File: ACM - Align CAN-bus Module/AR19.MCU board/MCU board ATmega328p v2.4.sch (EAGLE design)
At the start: 37 parts, among them IC1 ATMEGA328P-MMH, IC2 MIC5239-5.0YS_TR, IC3 MCP25625-E_ML, J1 AVR_SPI_PROG_3X2NS

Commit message: + SPI Priority | / 10K and 500Ohm to larger package | Smallest part 1206
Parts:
- removed C12, C13, C5, C6, C7, C8: 0.1uF, eagle-ltspice:CC0603
- removed R2: 10KΩ, CPF0201D10KC1:CPF0201D10KC1
- added C14, C15, C16, C17, C18, C19: 0.1uF_12, 12066D106KAT2A:12066D106KAT2A
- added R3, R4, R5: 500Ohm, CRCW1206499RFKEAHP(499ohm resistor):CRCW1206499RFKEAHP
- added R6: 10K Ohm, CRCW120610K0FKEAHP(10K Ohm):CRCW120610K0FKEAHP
- C11: value 0.1uF -> 0.1uF_12; device eagle-ltspice:CC0603 -> 12066D106KAT2A:12066D106KAT2A
- I/O_D2_INT: device wirepad:2,15/1,0 -> wirepad_edit:2,15/1,0(HALFHOLE)H+V
- R1: value 10KΩ -> 10K Ohm; device CPF0201D10KC1:CPF0201D10KC1 -> CRCW120610K0FKEAHP(10K Ohm):CRCW120610K0FKEAHP
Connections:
- removed net MISO: J1.1
- removed net MOSI: J1.4
- new net PROG_MISO: J1.1, R4.1
- new net PROG_MOSI: J1.4, R5.1
- new net PROG_SCK: J1.3, R3.1
- net 5V: now also C11.2, C14.2, C15.2, C17.2, C18.2, C19.2, R6.2; no longer C11.1, C12.1, C13.1, C6.1, C7.1, C8.1, R2.2
- net CAN_MISO: now also R4.2
- net CAN_MOSI: now also R5.2
- net GND: now also C11.1, C14.1, C15.1, C16.1, C17.1, C18.1, C19.1; no longer C11.2, C12.2, C13.2, C5.2, C6.2, C7.2, C8.2
- net MCP_RESET: now also C16.2, R1.1; no longer C5.1, R2.1
- net RESET_MCU: now also R6.1; no longer R1.1
- net SCK: now also R3.2; no longer J1.3
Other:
- note added: "SPI Priority"
- moved on the sheet: R1

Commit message: Updated BOM and SPI Priority
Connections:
- net CAN_MISO: now also R4.1; no longer IC1.(PCINT4/MISO)_PB4, R4.2
- net CAN_MOSI: now also R5.1; no longer IC1.(PCINT3/OC2A/MOSI)_PB3, R5.2
- net PROG_MISO: now also IC1.(PCINT4/MISO)_PB4, R4.2; no longer R4.1
- net PROG_MOSI: now also IC1.(PCINT3/OC2A/MOSI)_PB3, R5.2; no longer R5.1
- net PROG_SCK: now also IC1.PB5_(SCK/PCINT5), R3.2; no longer R3.1
- net SCK: now also R3.1; no longer IC1.PB5_(SCK/PCINT5), R3.2

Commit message: Byttet I/O pins, 0603 imp smd størrelse. Mangler dotstar support
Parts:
- removed C1, C4: 10uF, T491A106K016AT:T491A106K016AT
- removed C14, C15, C18, C19: 0.1uF_12, 12066D106KAT2A:12066D106KAT2A
- removed I/O_AD1, I/O_AD2, I/O_AD3, I/O_D0_RX, I/O_D1_TX, I/O_D2_INT: (no value), wirepad_edit:2,15/1,0(HALFHOLE)H+V
- removed R4, R5: 500Ohm, CRCW1206499RFKEAHP(499ohm resistor):CRCW1206499RFKEAHP
- removed R6: 10K Ohm, CRCW120610K0FKEAHP(10K Ohm):CRCW120610K0FKEAHP
- added C12, C13, C6, C7, C8: 0.1uF, eagle-ltspice:CC0603
- added C5: 22pF, eagle-ltspice:CC0603
- added D1: (no value), eagle-ltspice:DIODE_E-
- added I/O_PWM0_INT: I/O_PWM0_INT, wirepad_edit:2,15/1,0(HALFHOLE)H+V
- added I/O_PWM1: I/O_PWM1, wirepad_edit:2,15/1,0(HALFHOLE)H+V
- added I/O_PWM2: I/O_PWM2, wirepad_edit:2,15/1,0(HALFHOLE)H+V
- added MISO: MISO, wirepad_edit:2,15/1,0(HALFHOLE)H+V
- added MOSI: MOSI, wirepad_edit:2,15/1,0(HALFHOLE)H+V
- added SCK: SCK, wirepad_edit:2,15/1,0(HALFHOLE)H+V
- 12V: value (none) -> 12V
- C10: value 22pF -> 10uF; device 12066D106KAT2A:12066D106KAT2A -> eagle-ltspice:CC0603
- C11: value 0.1uF_12 -> 10uF; device 12066D106KAT2A:12066D106KAT2A -> eagle-ltspice:CC0603
- C16, C17: value 0.1uF_12 -> 0.1uF; device 12066D106KAT2A:12066D106KAT2A -> eagle-ltspice:CC0603
- C2, C3, C9: device 12066D106KAT2A:12066D106KAT2A -> eagle-ltspice:CC0603
- I/O_AD0: value (none) -> I/O_AD0
- I/O_CANH, I/O_CANL: value (none) -> I/O_CANH
- I/O_SCL_AD2: value (none) -> I/O_SCL_AD2
- I/O_SDA_AD1: value (none) -> I/O_SDA_AD1
- R1: value 10K Ohm -> 10kOhm; device CRCW120610K0FKEAHP(10K Ohm):CRCW120610K0FKEAHP -> eagle-ltspice:RR0603
- R3: value 500Ohm -> 10kOhm; device CRCW1206499RFKEAHP(499ohm resistor):CRCW1206499RFKEAHP -> eagle-ltspice:RR0603
- RES_PAD1: value (none) -> RES_PAD
- RES_PAD2: value (none) -> RES_PAD2
- renumbered I/O_AD4_SDA to I/O_SDA_AD1, I/O_AD5_SCL to I/O_SCL_AD2
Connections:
- net CAN_INIT renamed CAN_INT
- net I/O_AD4_SCL renamed N$6
- net I/O_AD5_SCL renamed N$7
- removed net CAN_MISO: IC3.SO, R4.1
- removed net CAN_MOSI: IC3.SI, R5.1
- removed net I/O_AD0: I/O_AD0.P, IC1.PC0_(ADC0/PCINT8)
- removed net I/O_AD1: I/O_AD1.P, IC1.PC1_(ADC1/PCINT9)
- removed net I/O_AD2: I/O_AD2.P, IC1.PC2_(ADC2/PCINT10)
- removed net I/O_AD3: I/O_AD3.P, IC1.PC3_(ADC3/PCINT11)
- removed net I/O_D0_RX: I/O_D0_RX.P, IC1.PD0_(RXD/PCINT16)
- removed net I/O_D1_TX: I/O_D1_TX.P, IC1.PD1_(TXD/PCINT17)
- removed net MCP_RESET: C16.2, IC3.RESET, R1.1
- removed net PROG_MISO: IC1.(PCINT4/MISO)_PB4, J1.1, R4.2
- removed net PROG_MOSI: IC1.(PCINT3/OC2A/MOSI)_PB3, J1.4, R5.2
- removed net PROG_SCK: IC1.PB5_(SCK/PCINT5), J1.3, R3.2
- new net MISO: IC1.(PCINT4/MISO)_PB4, IC3.SI, J1.1, MISO.P
- new net MOSI: IC1.(PCINT3/OC2A/MOSI)_PB3, IC3.SO, J1.4, MOSI.P
- new net N$1: IC3.RESET, R1.2
- new net N$2: I/O_PWM2.P, IC1.(PCINT21/OC0B/T1)_PD5
- new net N$3: I/O_PWM1.P, IC1.(PCINT20/XCK/T0)_PD4
- new net N$5: I/O_AD0.P, IC1.PC3_(ADC3/PCINT11)
- net 12V_FUSED: now also C10.1; no longer C4.A
- net 5V: now also C11.1, C12.1, C13.1, C16.1, C17.1, C6.1, C7.1, C8.1, D1.A, D1.C, R1.1, R3.2; no longer C1.K, C11.2, C14.2, C15.2, C17.2, C18.2, C19.2, R1.2, R6.2
- net CAN_CS: now also IC1.(PCINT23/AIN1)_PD7; no longer IC1.(PCINT1/OC1A)_PB1
- net CAN_OSC1: now also C5.1; no longer C9.2
- net CAN_OSC2: now also C2.1; no longer C10.2
- net DOTS_CS: no longer IC1.(PCINT0/CLKO/ICP1)_PB0
- net GND: now also C10.2, C11.2, C12.2, C13.2, C16.2, C17.2, C2.2, C3.2, C5.2, C6.2, C7.2, C8.2, C9.2; no longer C1.A, C10.1, C11.1, C14.1, C15.1, C16.1, C17.1, C18.1, C19.1, C2.1, C3.1, C4.K, C9.1
- net I/O_D2_INT: now also I/O_PWM0_INT.P; no longer I/O_D2_INT.P
- net MCU_OSC1: now also C3.1; no longer C2.2
- net MCU_OSC2: now also C9.1; no longer C3.2
- net RESET_MCU: now also R3.1; no longer R6.1
- net SCK: now also IC1.PB5_(SCK/PCINT5), J1.3, SCK.P; no longer R3.1
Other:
- note removed: "SPI Priority"
- moved on the sheet: I/O_AD0

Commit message: Changes in schematic
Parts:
- removed D1: (no value), eagle-ltspice:DIODE_E-
- removed DOTSTAR: COM-14608, APA102–2020:COM-14608
- removed I/O_PWM1: I/O_PWM1, wirepad_edit:2,15/1,0(HALFHOLE)H+V
- removed I/O_PWM2: I/O_PWM2, wirepad_edit:2,15/1,0(HALFHOLE)H+V
- removed U$1, U$2: FA-20H, FA-20H 16.0000MF20X-B:FA-20H
- added C1: 0.1uF, eagle-ltspice:CC0603
- added I/O_AD1: I/O_AD1, wirepad_edit:2,15/1,0(HALFHOLE)H+V
- added I/O_PWM0: I/O_PWM0, wirepad_edit:2,15/1,0(HALFHOLE)H+V
- added LED1: SMLP36RGB2W3R, SMLP36RGB2W3R:SMLP36RGB2W3R
- added R10, R2, R6, R7, R8, R9: 200Ohm, eagle-ltspice:RR0603
- added R4: 290Ohm, eagle-ltspice:RR0603
- added R5: 190Ohm, eagle-ltspice:RR0603
- added U1, U2: CSTNE16M0V530000R0, CSTNE16M0V530000R0:CSTNE16M0V530000R0
- I/O_ADC2_SDA: value I/O_SDA_AD1 -> I/O_ADC2_SDA
- I/O_ADC3_SCL: value I/O_SCL_AD2 -> I/O_ADC3_SCL
- renumbered I/O_PWM0_INT to I/O_PWM1_INT1, I/O_SCL_AD2 to I/O_ADC3_SCL, I/O_SDA_AD1 to I/O_ADC2_SDA
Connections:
- removed net DOTS_CS: DOTSTAR.DIN
- new net BLUE_LED: IC1.(PCINT1/OC1A)_PB1, R5.1
- new net GREEN_LED: IC1.(PCINT22/OC0A/AIN0)_PD6, R2.1
- new net N$10: R6.2, SCK.P
- new net N$11: MISO.P, R7.2
- new net N$12: MOSI.P, R8.2
- new net N$4: LED1.ANODE_B, R2.2
- new net N$8: LED1.ANODE_R, R4.2
- new net N$9: LED1.ANODE_G, R5.2
- new net RED_LED: IC1.(PCINT21/OC0B/T1)_PD5, R4.1
- new net VOLTAGE_CHECK: C1.1, IC1.PC0_(ADC0/PCINT8), R10.2, R9.1
- net 12V_FUSED: now also R9.2
- net 5V: now also LED1.CATHODE_B, LED1.CATHODE_G, LED1.CATHODE_R; no longer D1.A, D1.C, DOTSTAR.VCC
- net CAN_OSC1: now also U1.INPUT; no longer U$1.1
- net CAN_OSC2: now also U1.OUTPUT; no longer U$1.3
- net GND: now also C1.2, R10.1, U1.GND, U2.GND; no longer DOTSTAR.GND
- net MCU_OSC1: now also U2.INPUT; no longer U$2.1
- net MCU_OSC2: now also U2.OUTPUT; no longer U$2.3
- net MISO: now also R7.1; no longer MISO.P
- net MOSI: now also R8.1; no longer MOSI.P
- net N$2: now also I/O_PWM0.P, IC1.(PCINT2/SS/OC1B)_PB2; no longer I/O_PWM2.P, IC1.(PCINT21/OC0B/T1)_PD5
- net N$3: now also I/O_AD1.P, IC1.PC2_(ADC2/PCINT10); no longer I/O_PWM1.P, IC1.(PCINT20/XCK/T0)_PD4
- net SCK: now also R6.1; no longer DOTSTAR.CIN, SCK.P

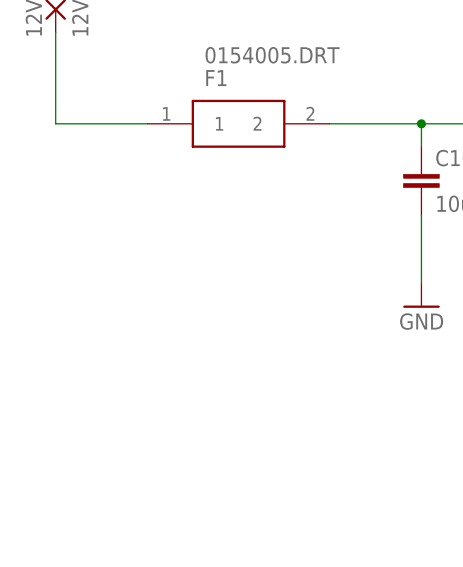
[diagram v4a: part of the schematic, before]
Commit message: Added GND I/O pin XD
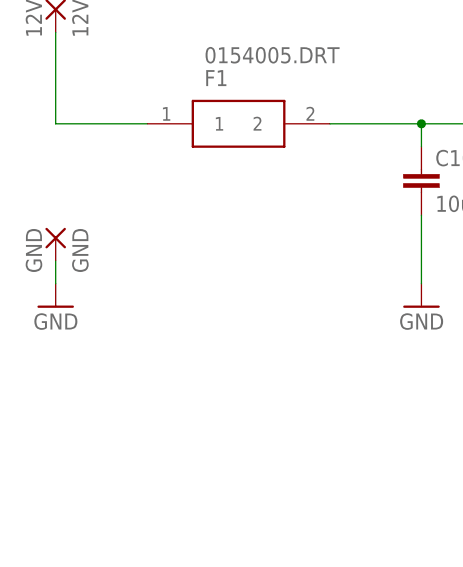
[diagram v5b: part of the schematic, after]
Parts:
- added GND: GND, wirepad:2,54/1,0
- 12V, I/O_AD0, I/O_AD1, I/O_ADC2_SDA, I/O_ADC3_SCL, I/O_CANH, I/O_CANL, I/O_PWM0, I/O_PWM1_INT1, MISO, MOSI, SCK: device wirepad_edit:2,15/1,0(HALFHOLE)H+V -> wirepad:2,54/1,0
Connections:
- net GND: now also GND.P

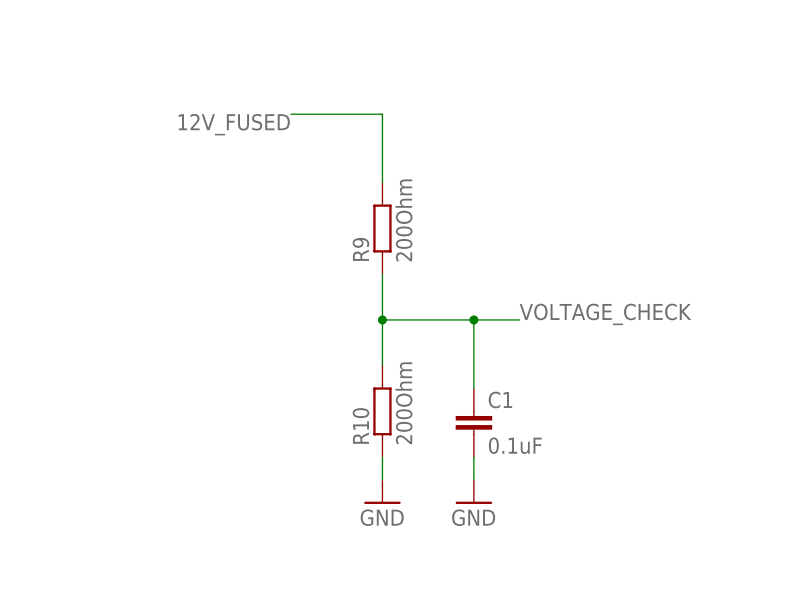
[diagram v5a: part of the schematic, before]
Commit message: Voltage divider resistor changed
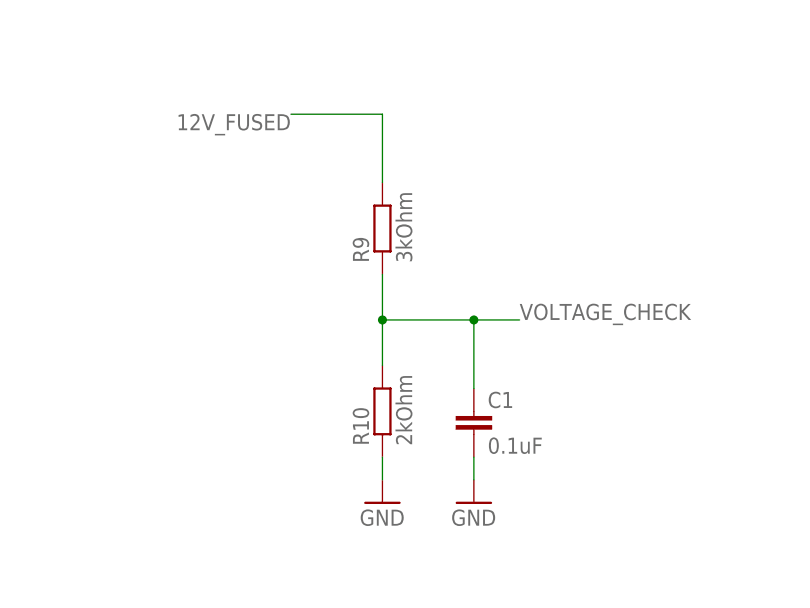
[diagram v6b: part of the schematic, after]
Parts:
- R10: value 200Ohm -> 2kOhm
- R9: value 200Ohm -> 3kOhm
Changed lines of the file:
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@@
 <part name="R7" library="eagle-ltspice" library_urn="urn:adsk.eagle:library:217" deviceset="R" device="R0603" package3d_urn="urn:adsk.eagle:package:13302/1" value="200Ohm"/>
 <part name="R8" library="eagle-ltspice" library_urn="urn:adsk.eagle:library:217" deviceset="R" device="R0603" package3d_urn="urn:adsk.eagle:package:13302/1" value="200Ohm"/>
-<part name="R9" library="eagle-ltspice" library_urn="urn:adsk.eagle:library:217" deviceset="R" device="R0603" package3d_urn="urn:adsk.eagle:package:13302/1" value="200Ohm"/>
-<part name="R10" library="eagle-ltspice" library_urn="urn:adsk.eagle:library:217" deviceset="R" device="R0603" package3d_urn="urn:adsk.eagle:package:13302/1" value="200Ohm"/>
+<part name="R9" library="eagle-ltspice" library_urn="urn:adsk.eagle:library:217" deviceset="R" device="R0603" package3d_urn="urn:adsk.eagle:package:13302/1" value="3kOhm"/>
+<part name="R10" library="eagle-ltspice" library_urn="urn:adsk.eagle:library:217" deviceset="R" device="R0603" package3d_urn="urn:adsk.eagle:package:13302/1" value="2kOhm"/>
 <part name="GND4" library="supply1" library_urn="urn:adsk.eagle:library:371" deviceset="GND" device=""/>
 <part name="GND28" library="supply1" library_urn="urn:adsk.eagle:library:371" deviceset="GND" device=""/>
